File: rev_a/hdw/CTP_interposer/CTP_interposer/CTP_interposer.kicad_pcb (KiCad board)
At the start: 2 copper layers, 10.7 x 31.8 mm, 2 parts, among them J2102 LCD CTP Data

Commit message: flex PCB layout
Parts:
- J2102: moved to F.Cu
- moved J2102 3.00 mm to (152.4, 71.1), turned to 0 degrees
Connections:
- J2102 pad 6: LCD _CTP_RESET -> LCD_CTP_RESET
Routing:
- net LCD_CTP_RESET: track 0.00 -> 26.8 mm, vias 0 -> 2
- net I2C_SCL: track 0.00 -> 26.8 mm, vias 0 -> 2
- net +3.0V: track 0.00 -> 26.8 mm, vias 0 -> 2
- net I2C_SDA: track 0.00 -> 26.8 mm, vias 0 -> 2
- net LCD_CTP_INT: track 0.00 -> 26.8 mm, vias 0 -> 2
- net GND: track 0.00 -> 2.68 mm, vias 0 -> 37
- added copper zone on B.Cu, net GND
- added copper zone on F.Cu, net GND
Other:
- board size 10.7 x 31.8 mm -> 10.7 x 30.4 mm
- board text added: "Gold Fingers on top copper"

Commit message: finished CTP flex PCB
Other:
- board text added: "2x polyimide stiffeners 0.2mm thickness Attached to flex PCB bottom Adhesive-bonded"

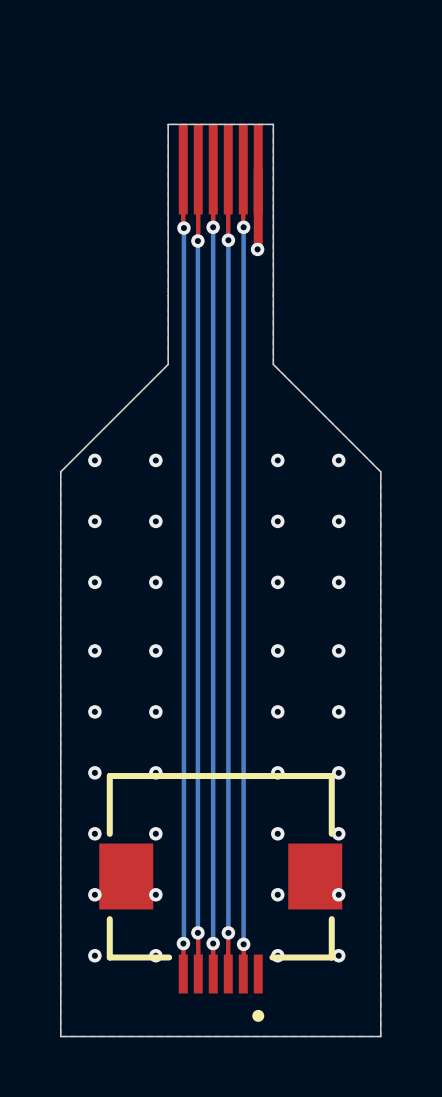
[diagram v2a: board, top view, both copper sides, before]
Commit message: fixed connector orientation and pinout
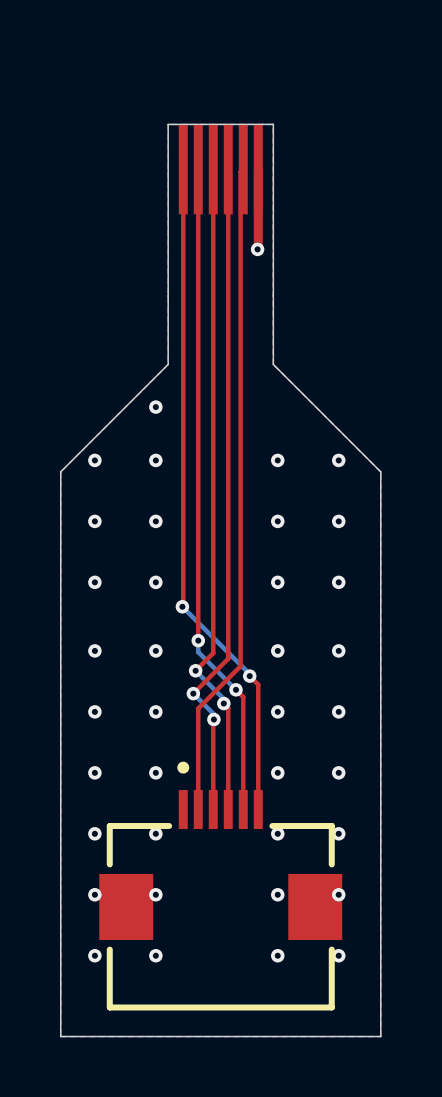
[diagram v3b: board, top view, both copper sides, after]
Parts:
- moved J2102 1.02 mm to (152.4, 92.5), turned to 0 degrees
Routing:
- net I2C_SCL: track 26.8 -> 22.0 mm
- net +3.0V: track 26.8 -> 22.0 mm, vias 2 -> 0
- net I2C_SDA: track 26.8 -> 22.0 mm
- net LCD_CTP_INT: track 26.8 -> 22.1 mm
- net LCD_CTP_RESET: track 26.8 -> 22.4 mm
- net GND: vias 37 -> 38
